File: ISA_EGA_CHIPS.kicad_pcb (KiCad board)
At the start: 2 copper layers, 131.1 x 108 mm, 67 parts, among them J1 EGA Feature Connector, J2 Light Pen, J3 RCA 1, J4 RCA 2, J6 Digital Output, J7 Bus_ISA_8bit, SW1 Configuration, U1 41464, U10 27C256, U11 82A436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

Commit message: Place some more components
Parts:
- moved U11 449.0 mm to (255.8, 176.0), turned to 90 degrees
- moved J1 0.76 mm to (310.4, 98.8)
- moved J2 0.76 mm to (310.4, 104.9)
- moved OSC1 0.76 mm to (265.9, 140.7)
- moved OSC2 0.76 mm to (265.9, 155.4)
- moved U4 0.76 mm to (270.8, 115.6)
- moved U6 0.76 mm to (273.3, 127.0)
- moved JP3 0.76 mm to (260.4, 134.4)

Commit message: Place some more components
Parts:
- moved SIP3 491.6 mm to (293.6, 161.0), turned to 270 degrees
- moved SIP4 465.2 mm to (297.7, 161.0), turned to 270 degrees
- moved C17 456.3 mm to (297.7, 151.1), turned to 90 degrees
- moved C9 455.0 mm to (289.3, 137.2), turned to 270 degrees
- moved C90 448.4 mm to (297.4, 156.5), turned to 180 degrees
- moved C25 434.7 mm to (288.0, 182.9), turned to 90 degrees
- moved C20 415.5 mm to (288.0, 162.6), turned to 270 degrees
- moved C12 390.0 mm to (297.7, 137.2), turned to 270 degrees
- moved C16 389.6 mm to (294.9, 146.1), turned to 270 degrees
- moved C11 387.7 mm to (294.9, 137.2), turned to 270 degrees
- moved C10 384.0 mm to (292.1, 137.2), turned to 270 degrees
- moved C40 381.6 mm to (287.0, 190.0)
- moved C15 380.7 mm to (292.1, 151.1), turned to 90 degrees
- moved C28 371.1 mm to (295.9, 190.0)
- moved C26 366.4 mm to (264.4, 224.3)
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
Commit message: Placed all components
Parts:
- moved JP2 435.8 mm to (250.4, 170.7)
- moved U10 425.3 mm to (216.4, 159.0), turned to 90 degrees
- moved SIP1 410.1 mm to (254.0, 110.5), turned to 270 degrees
- moved R4 400.9 mm to (269.0, 101.9), turned to 180 degrees
- moved U13 384.6 mm to (220.0, 173.0), turned to 90 degrees
- moved R5 380.1 mm to (260.4, 147.6), turned to 270 degrees
- moved U15 378.8 mm to (220.0, 184.4), turned to 90 degrees
- moved R3 370.0 mm to (269.0, 98.6), turned to 180 degrees
- moved JP10 369.3 mm to (264.7, 105.7), turned to 270 degrees
- moved R1 358.6 mm to (215.9, 97.3)
- moved C24 355.8 mm to (216.9, 178.1), turned to 270 degrees
- moved U8 354.2 mm to (189.2, 154.9), turned to 90 degrees
- moved U9 346.9 mm to (189.2, 166.9), turned to 90 degrees
- moved C7 346.0 mm to (270.3, 120.7), turned to 270 degrees
- moved U2 340.4 mm to (233.4, 105.7)
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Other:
- net class POWER added: clearance 0.25, trace_width 0.5, via_dia 0.8, via_drill 0.4
- net class POWER_SMALL added: clearance 0.25, trace_width 0.35, via_dia 0.8, via_drill 0.4

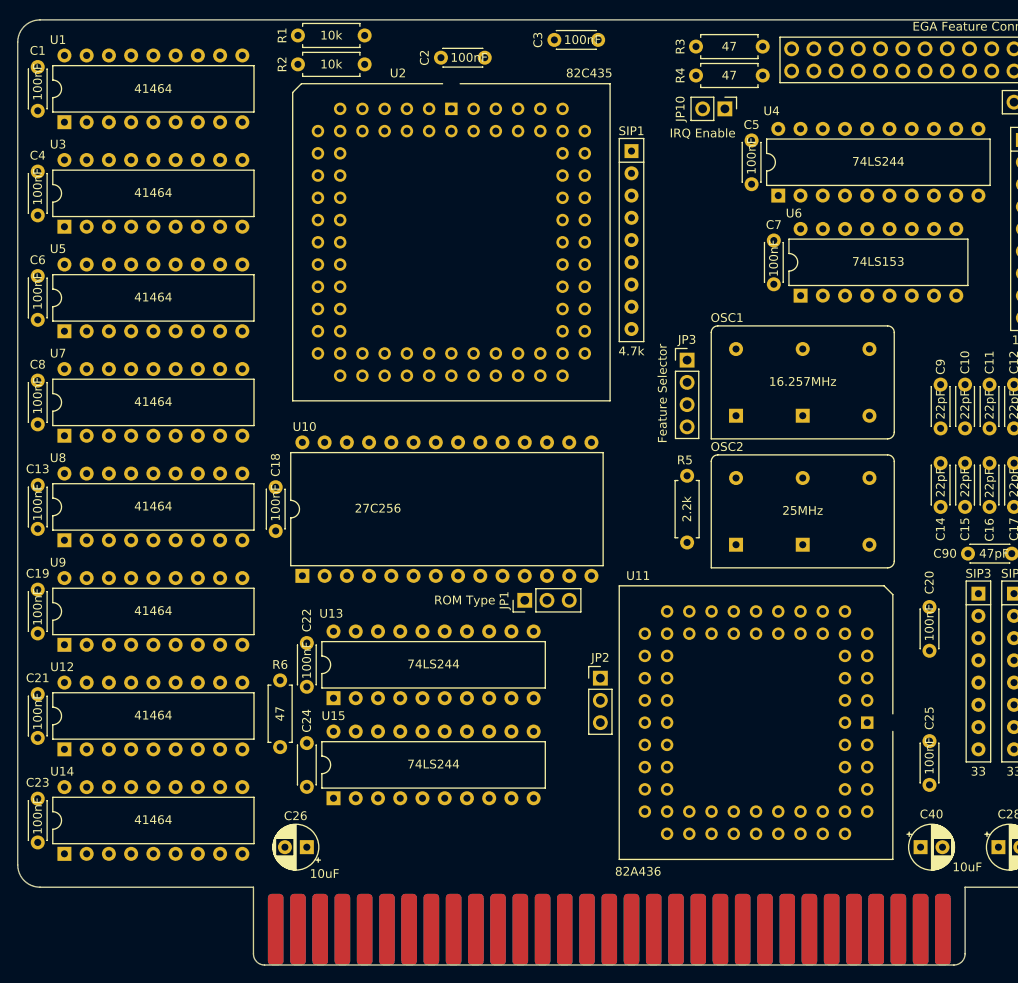
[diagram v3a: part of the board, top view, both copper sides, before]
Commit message: Draw basic power traces
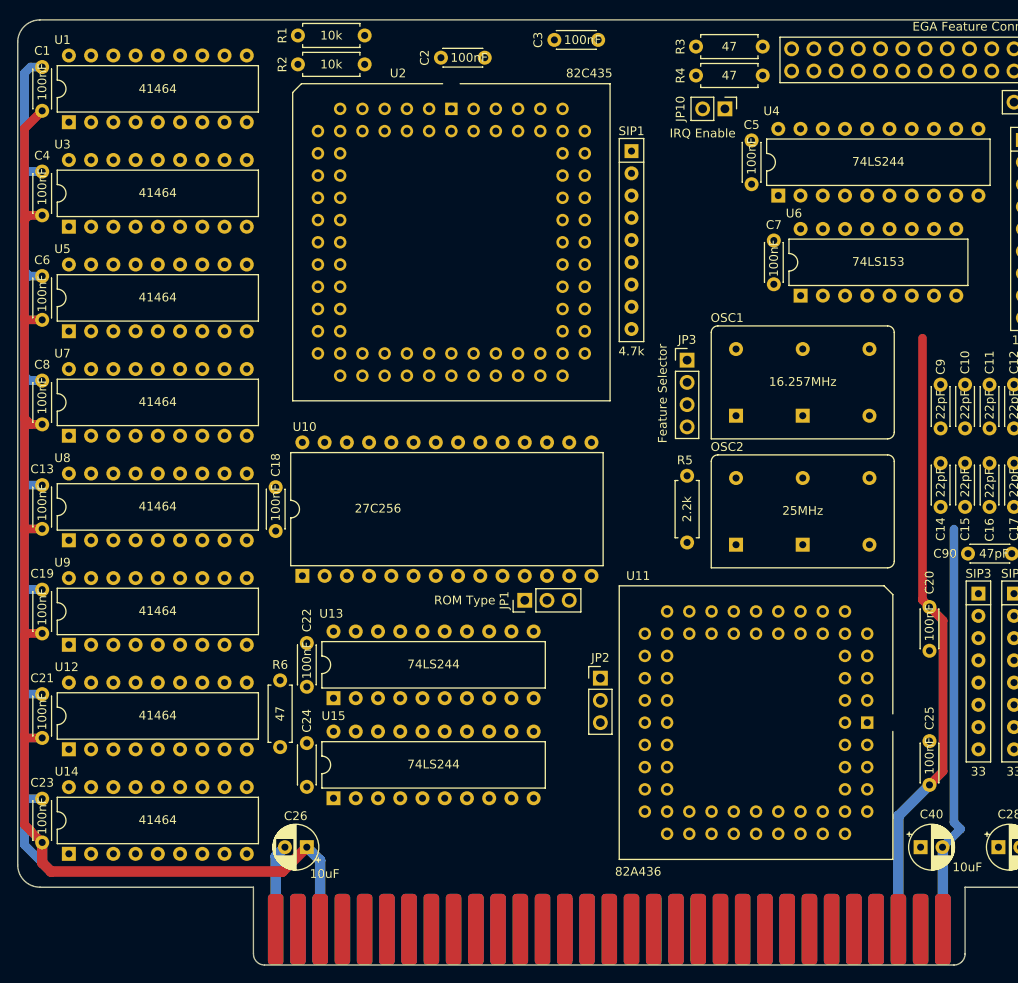
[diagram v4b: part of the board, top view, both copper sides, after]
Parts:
- moved C6 5.03 mm to (186.7, 129.8), turned to 90 degrees
- moved C1 0.51 mm to (186.7, 105.9)
- moved C13 0.51 mm to (186.7, 153.6)
- moved C19 0.51 mm to (186.7, 165.6)
- moved C21 0.51 mm to (186.7, 177.5)
- moved C23 0.51 mm to (186.7, 189.5)
- moved C4 0.51 mm to (186.7, 117.8)
- moved C8 0.51 mm to (186.7, 141.7)
- moved U1 0.51 mm to (189.7, 107.2)
- moved U12 0.51 mm to (189.7, 178.8)
- moved U14 0.51 mm to (189.7, 190.8)
- moved U3 0.51 mm to (189.7, 119.1)
- moved U5 0.51 mm to (189.7, 131.1)
- moved U7 0.51 mm to (189.7, 143.0)
- moved U8 0.51 mm to (189.7, 154.9)
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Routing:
- net VCC: track 0.00 -> 213.7 mm
- net GND: track 0.00 -> 192.0 mm

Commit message: First board render
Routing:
- net GND: track 192.0 -> 863.9 mm
- net VCC: track 213.7 -> 813.6 mm, vias 0 -> 6
- net /BUS_OSC: track 0.00 -> 190.8 mm, vias 0 -> 5
- net +12V: track 0.00 -> 186.3 mm, vias 0 -> 3
- net /BUF_VIN: track 0.00 -> 180.9 mm
- net /IOADS: track 0.00 -> 177.0 mm, vias 0 -> 3
- net /~RAS: track 0.00 -> 169.2 mm, vias 0 -> 2
- net /~IO_RDY: track 0.00 -> 165.5 mm, vias 0 -> 3
- net /BUF_A01: track 0.00 -> 152.2 mm, vias 0 -> 2
- net /BUF_A03: track 0.00 -> 149.0 mm, vias 0 -> 3
- net /BUF_A07: track 0.00 -> 145.1 mm, vias 0 -> 2
- net /LPENSTB: track 0.00 -> 144.1 mm, vias 0 -> 5
- net /BUF_A15: track 0.00 -> 142.6 mm, vias 0 -> 4
- net /BUF_A02: track 0.00 -> 139.5 mm, vias 0 -> 2
- net /BS_V: track 0.00 -> 138.9 mm, vias 0 -> 2
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- added copper zone on B.Cu, net GND
- added copper zone on F.Cu, net GND

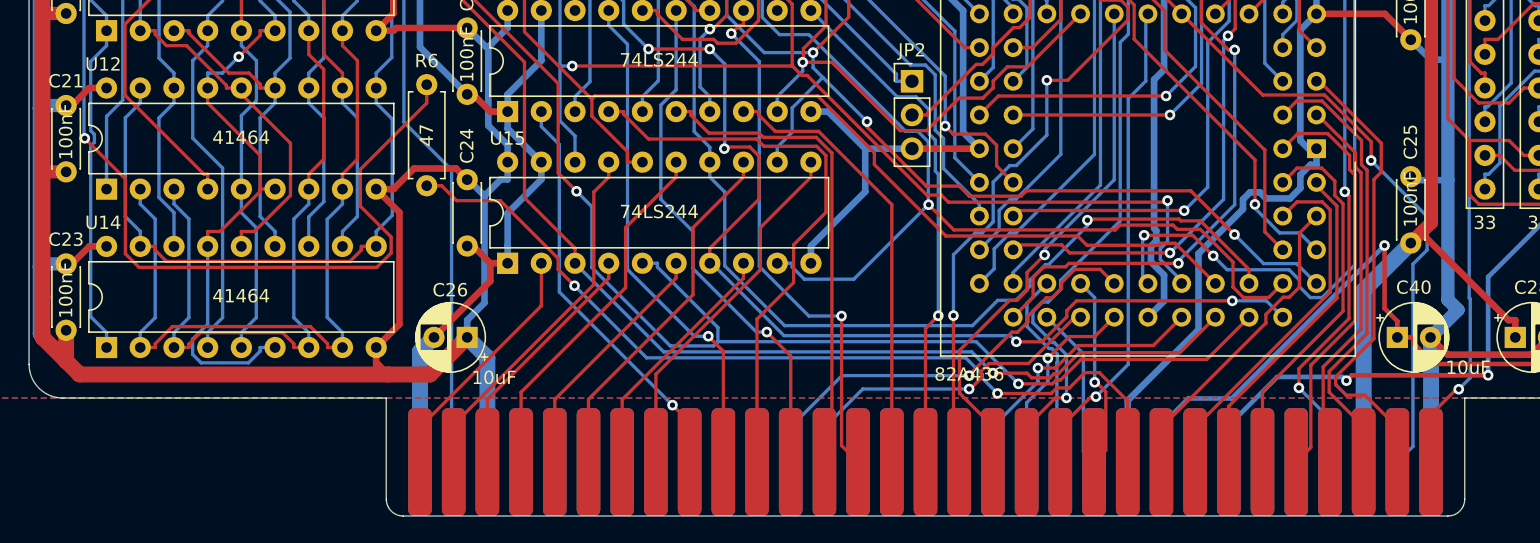
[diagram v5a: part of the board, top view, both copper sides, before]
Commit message: Add silkscreen
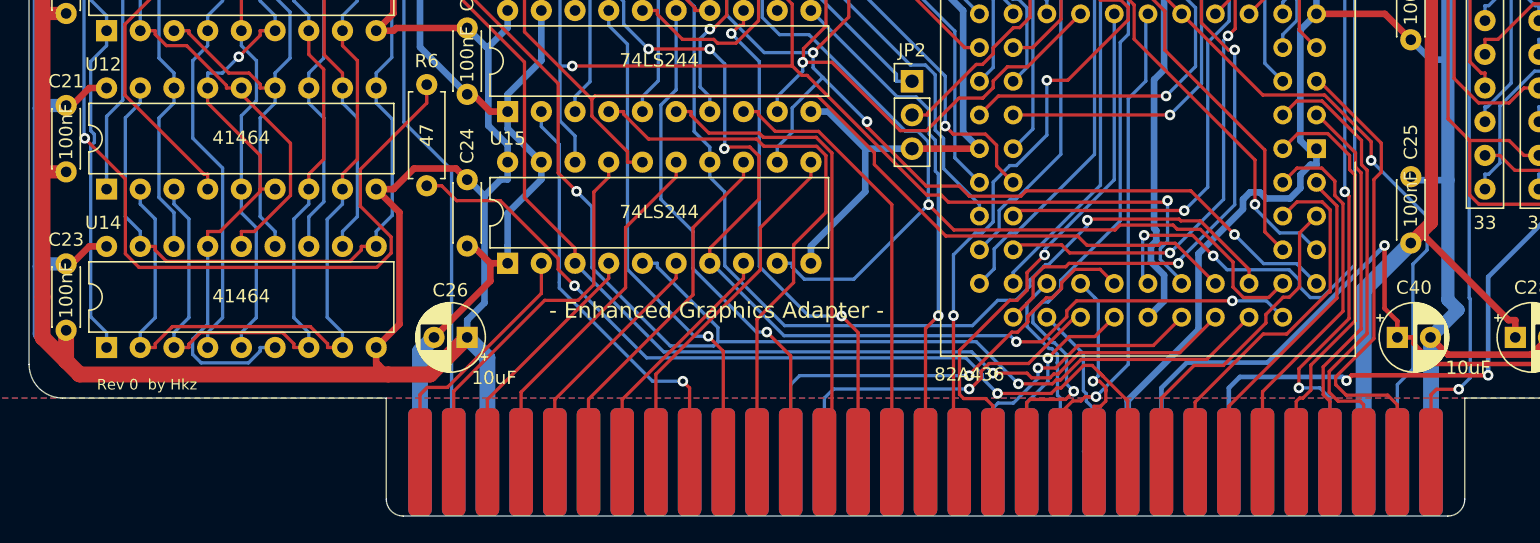
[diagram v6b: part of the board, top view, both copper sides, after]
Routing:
- net /BUS_A19: track 36.7 -> 44.2 mm
- net Net-(C90-Pad2): track 125.1 -> 129.7 mm
- net /BUS_CLK: track 32.9 -> 37.4 mm
- net +12V: track 186.3 -> 190.7 mm
- net -12V: track 125.5 -> 130.0 mm
- net /BUS_A08: track 31.0 -> 35.4 mm
- net /BUS_A01: track 27.4 -> 31.7 mm
- net /BUS_A18: track 42.8 -> 47.0 mm
- net Net-(J7-Pad4): track 107.5 -> 111.7 mm
- net /~DACK0: track 25.7 -> 29.6 mm
- net /BUS_D0: track 23.7 -> 27.6 mm
- net /BUS_D1: track 27.5 -> 31.3 mm
- net /BUS_A17: track 40.0 -> 43.6 mm
- net /BUS_D6: track 34.3 -> 37.9 mm
- net /BUS_D7: track 35.0 -> 38.7 mm
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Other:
- board text added: "- Enhanced Graphics Adapter -"
- board text added: "Rev 0 by Hkz"

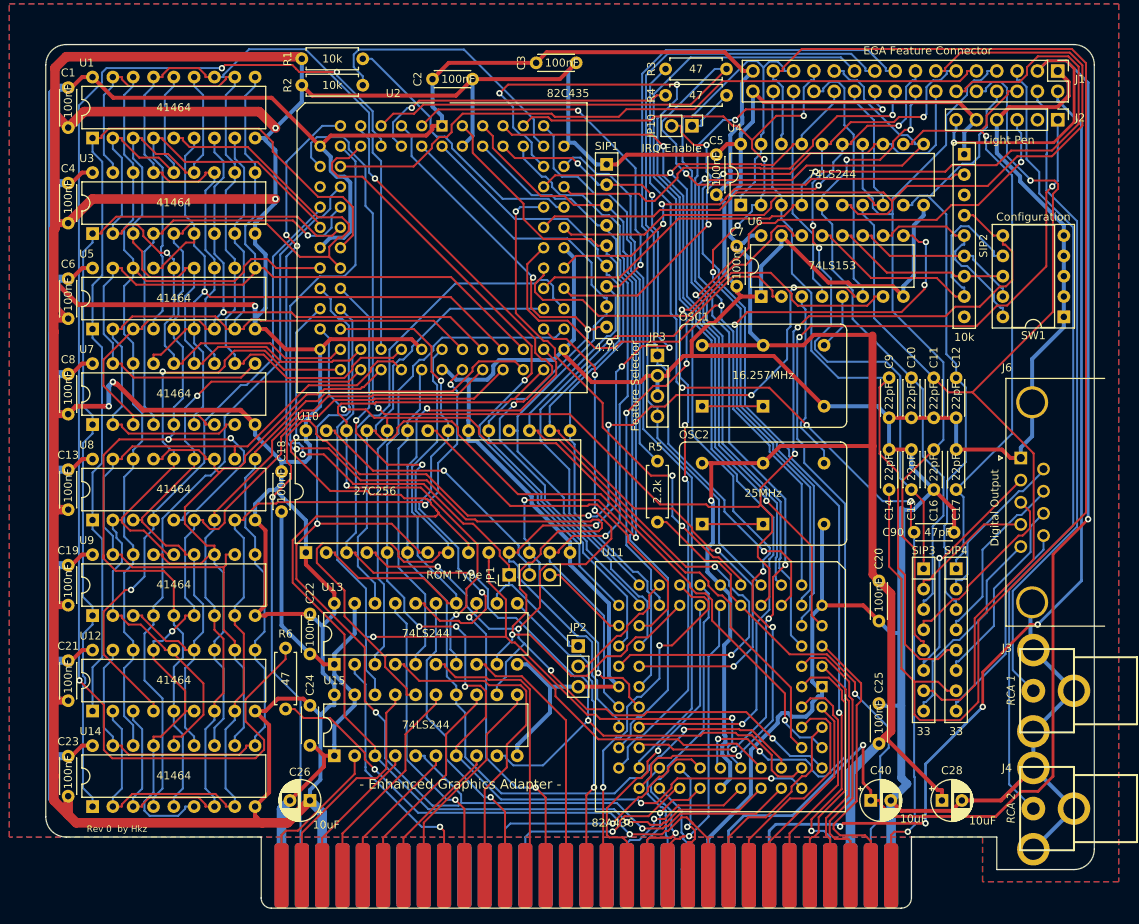
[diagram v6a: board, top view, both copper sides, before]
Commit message: Cleaned board, redone power traces
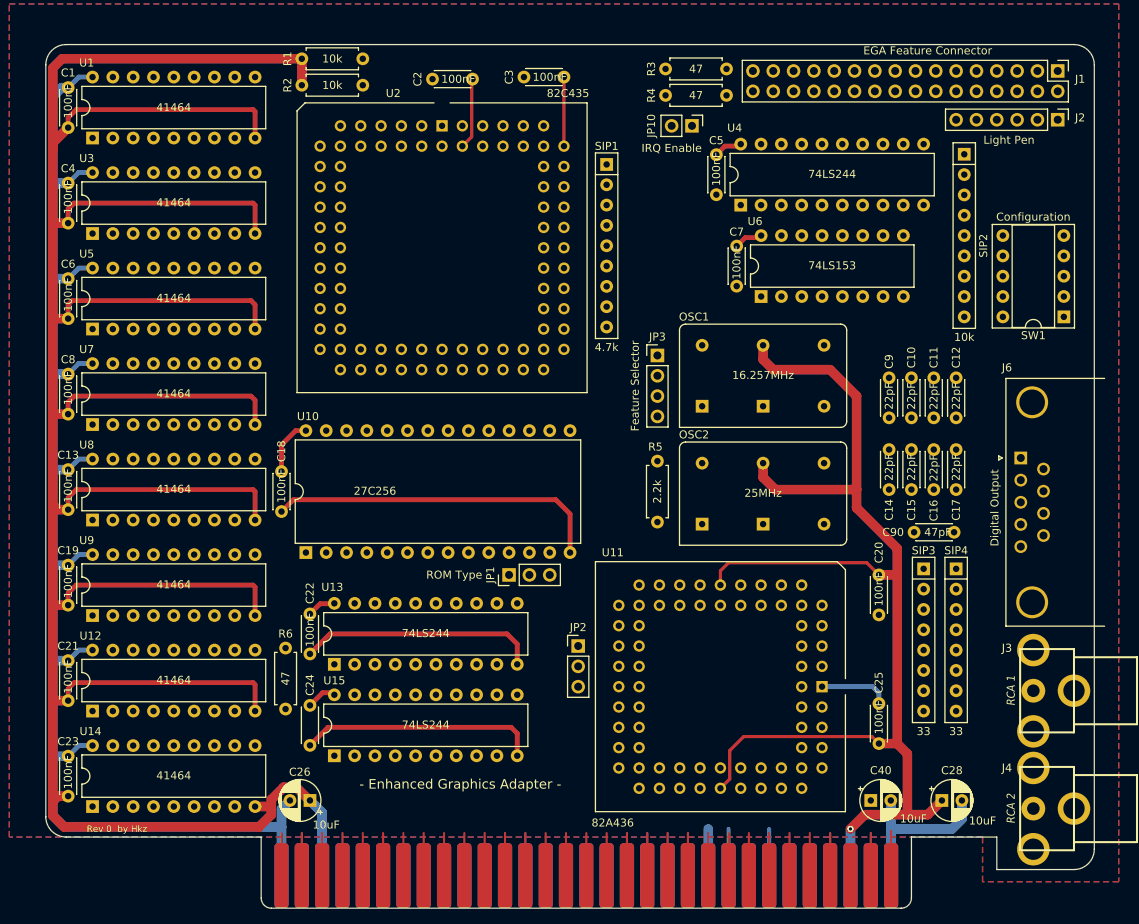
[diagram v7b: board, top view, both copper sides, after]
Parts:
- moved C3 2.34 mm to (248.7, 99.6)
- moved C20 0.76 mm to (288.0, 161.8)
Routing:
- net GND: track 863.9 -> 312.3 mm
- net VCC: track 813.6 -> 590.4 mm, vias 6 -> 1
- net /BUS_OSC: track 190.8 -> 5.33 mm, vias 5 -> 0
- net +12V: track 190.7 -> 5.84 mm, vias 3 -> 0
- net /BUF_VIN: track 180.9 -> 0.00 mm
- net /IOADS: track 177.0 -> 0.00 mm, vias 3 -> 0
- net /~RAS: track 169.2 -> 0.00 mm, vias 2 -> 0
- net /~IO_RDY: track 165.5 -> 0.00 mm, vias 3 -> 0
- net /BUF_A01: track 152.2 -> 0.00 mm, vias 2 -> 0
- net /BUF_A03: track 149.0 -> 0.00 mm, vias 3 -> 0
- net /BUF_A07: track 145.1 -> 0.00 mm, vias 2 -> 0
- net /LPENSTB: track 144.1 -> 0.00 mm, vias 5 -> 0
- net /BUF_A15: track 142.6 -> 0.00 mm, vias 4 -> 0
- net /BUF_A02: track 139.5 -> 0.00 mm, vias 2 -> 0
- net /BS_V: track 138.9 -> 0.00 mm, vias 2 -> 0
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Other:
- net class POWER: trace_width 0.5 -> 0.6

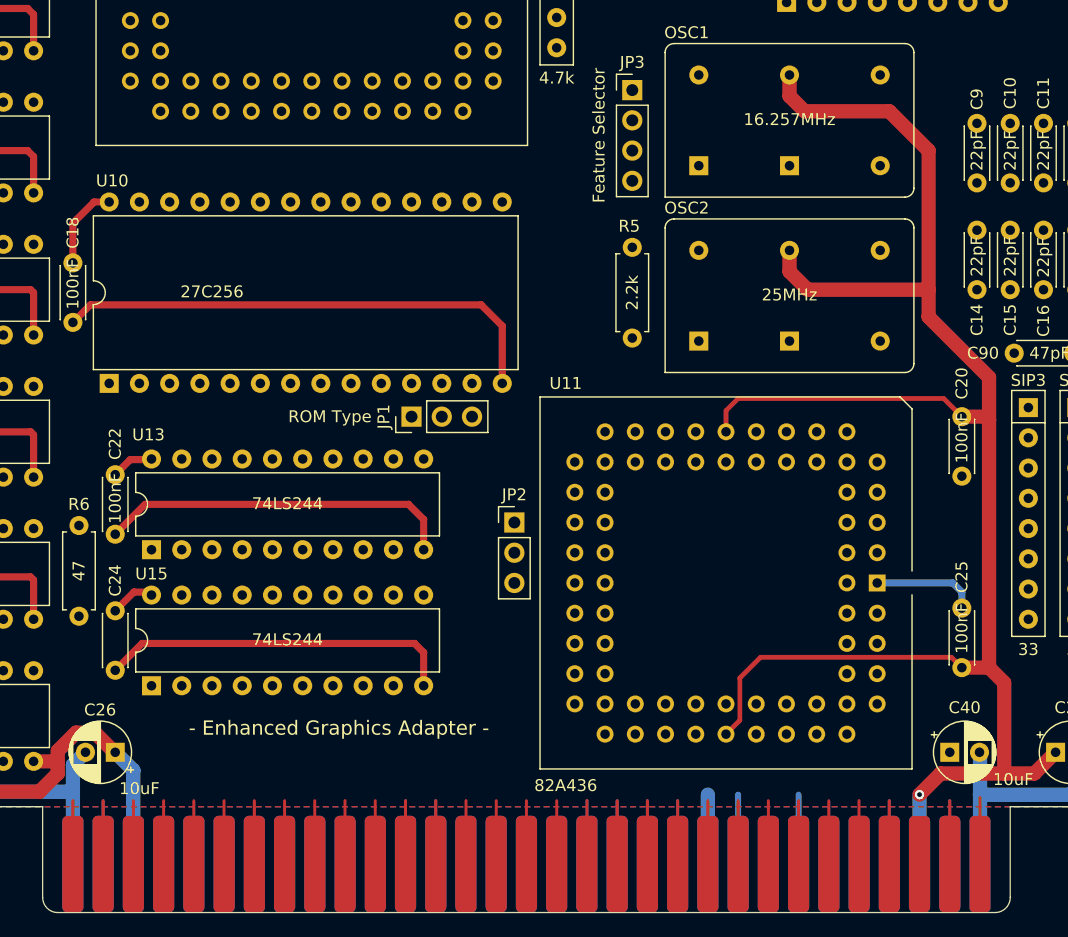
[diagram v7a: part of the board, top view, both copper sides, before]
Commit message: moved around some components
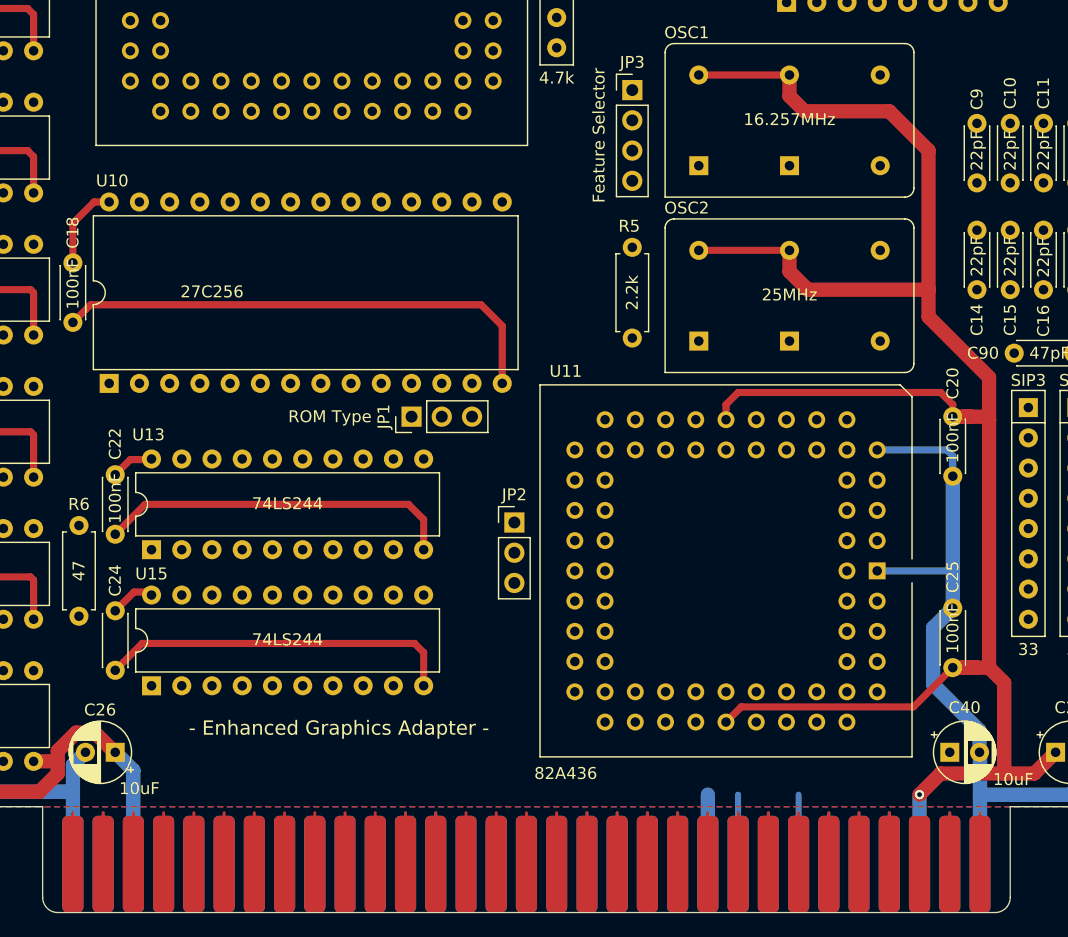
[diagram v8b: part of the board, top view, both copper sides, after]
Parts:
- moved U11 1.02 mm to (280.9, 174.8)
- moved C20 0.76 mm to (287.3, 161.8)
- moved C25 0.76 mm to (287.3, 182.9)
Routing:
- net GND: track 312.3 -> 343.7 mm
- net VCC: track 590.4 -> 604.8 mm
- net (no net): track 0.00 -> 13.0 mm
- net Net-(C90-Pad2): track 5.59 -> 4.32 mm
- net Net-(J7-Pad41): track 5.33 -> 4.32 mm
- net Net-(J7-Pad4): track 5.33 -> 4.32 mm
- net /~MEMW: track 5.33 -> 4.32 mm
- net /~MEMR: track 5.33 -> 4.32 mm
- net /~IOW: track 5.33 -> 4.32 mm
- net /~IOR: track 5.33 -> 4.32 mm
- net /~DACK0: track 5.33 -> 4.32 mm
- net /RESET: track 5.33 -> 4.32 mm
- net /BUS_OSC: track 5.33 -> 4.32 mm
- net /BUS_D7: track 5.33 -> 4.32 mm
- net /BUS_D5: track 5.33 -> 4.32 mm
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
